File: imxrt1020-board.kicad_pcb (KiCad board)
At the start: 2 copper layers, 102.9 x 68.6 mm, 187 parts, among them J1 Micro_SD_Card_Det, J10 CASTELATED, J11 CASTELATED, J12 CASTELATED, J13 CASTELATED, J14 CASTELATED, J15 CASTELATED, J16 CASTELATED, J17 CASTELATED, J18 CASTELATED, J19 CASTELATED, J2 USB_OTG, J20 CASTELATED, J21 CASTELATED, J22 CASTELATED, J23 CASTELATED, J24 CASTELATED, J25 CASTELATED, J26 CASTELATED, J27 CASTELATED, J28 CASTELATED, J29 CASTELATED, J3 Conn_02x20_Odd_Even, J30 CASTELATED, J31 CASTELATED, J32 CASTELATED, J33 CASTELATED, J34 CASTELATED, J35 CASTELATED, J36 CASTELATED, J37 CASTELATED, J38 CASTELATED, J39 CASTELATED, J4 CASTELATED, J40 CASTELATED, J41 CASTELATED, J42 CASTELATED, J43 CASTELATED, J44 GS2, J45 GS2, J46 PWR_IN, J47 JTAG, J48 Conn_01x06, J49 CASTELATED, J5 CASTELATED, J50 CASTELATED, J51 CASTELATED, J52 CASTELATED, J53 CASTELATED, J54 CASTELATED, J55 CASTELATED, J56 CASTELATED, J57 CASTELATED, J58 RJ45-TRANSFO, J59 CASTELATED, J6 CASTELATED, J60 CASTELATED, J61 CASTELATED, J62 CASTELATED, J63 CASTELATED, J64 CASTELATED, J65 CASTELATED, J66 CASTELATED, J67 CASTELATED, J68 CASTELATED, J7 CASTELATED, J8 CASTELATED, J9 CASTELATED, SW1 RST, SW2 SW_DIP_x02, SW3 WAKE, U1 imx_rt1020-qfp144, U2 M25PX32-VMW, U3 AS4C16M16S, U4 TPS3839DBZ, U5 LM1084-3.3, U6 ISL3178E, U7 KSZ8081RNA, U8 TCAN332D, Y1 24MHz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

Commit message: Add USB EMI filter, more silkscreen enances
Signed-off-by: Martin Ribelotta <martinribelotta@gmail.com>
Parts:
- added U9: NUF2221W1http, TO_SOT_Packages_SMD:SOT-363_SC-70-6, F.Cu at (116.1, 117.8)
- moved J44 6.09 mm to (116.9, 127.7), turned to 90 degrees
- moved J45 4.14 mm to (116.9, 122.7), turned to 270 degrees
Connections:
- U1 pad 62: /GPIO/OTG_D- -> /GPIO/A_OTG_D-
- U1 pad 63: /GPIO/OTG_D+ -> /GPIO/A_OTG_D+
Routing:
- net +3V3: track 588.6 -> 643.7 mm, vias 3 -> 5
- net /GPIO/OTG_D-: track 60.1 -> 20.2 mm, vias 2 -> 1
- net /GPIO/A_OTG_D-: track 0.00 -> 38.9 mm, vias 0 -> 2
- net /GPIO/OTG_D+: track 59.8 -> 21.1 mm, vias 2 -> 1
- net /GPIO/A_OTG_D+: track 0.00 -> 37.5 mm, vias 0 -> 2
- net GND: track 451.0 -> 466.3 mm, vias 284 -> 280
- net /POWER/PWR_IN1: track 12.0 -> 17.5 mm, vias 6 -> 7
- net +5V: track 37.9 -> 41.3 mm
- net /GPIO/DC_IN: track 5.26 -> 5.93 mm
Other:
- board text added: "+5V +3v3 IO31 IO30 IO29 IO28 IO27 IO26 IO25 IO24 IO23 IO22 IO21 IO20 IO19 IO18 IO17 IO16 IO07 IO06"
- board text removed: "IO31 IO30 IO29 IO28 IO27 IO26 IO25 IO24 IO23 IO22 IO21 IO20 IO19 IO18 IO17 IO16 IO07 IO06"

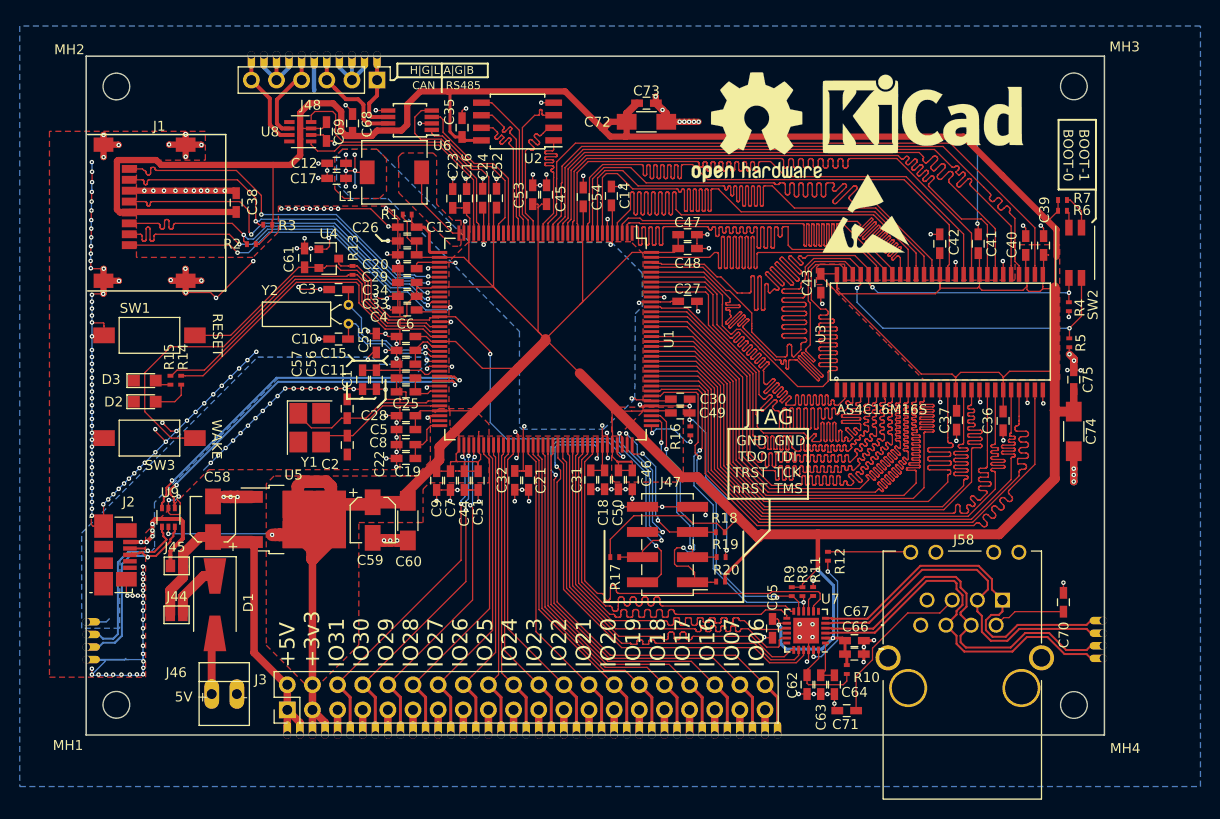
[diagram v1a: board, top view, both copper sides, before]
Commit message: Minor changes on PCB
Signed-off-by: Martin Ribelotta <martinribelotta@gmail.com>
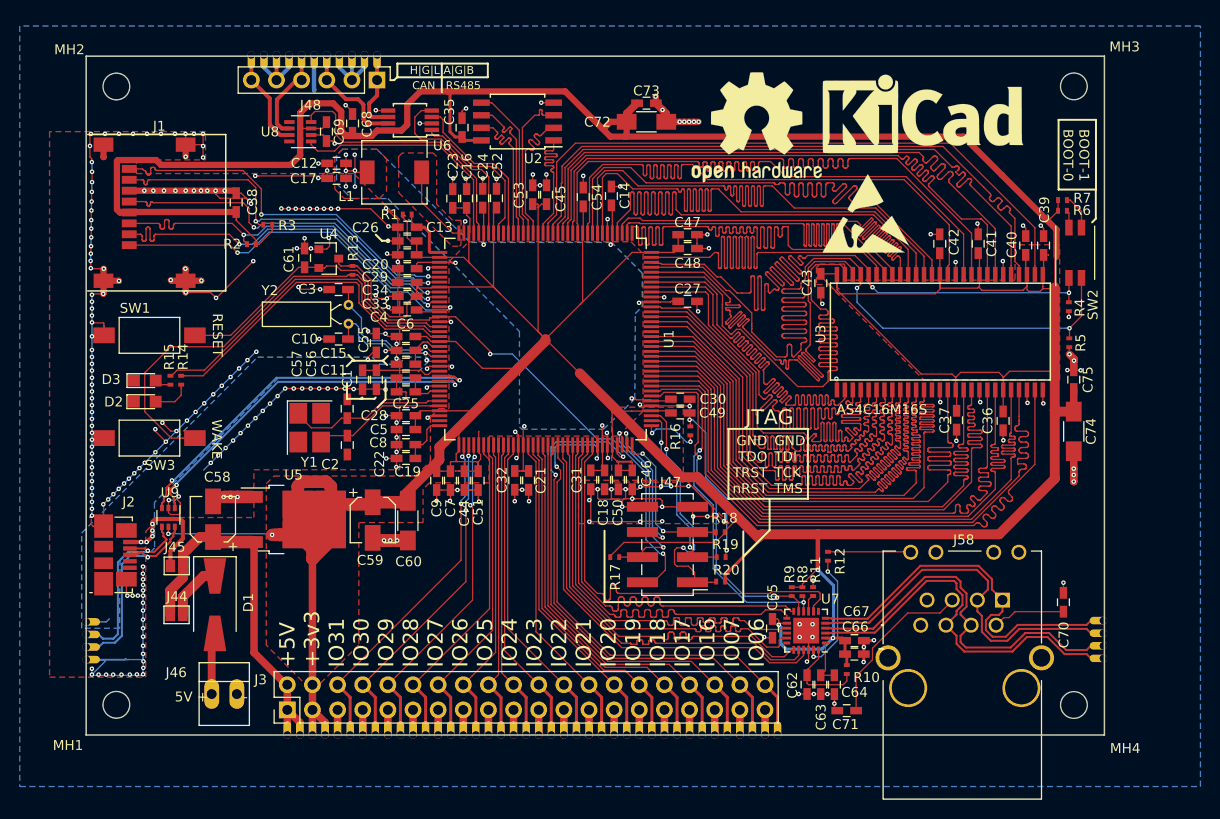
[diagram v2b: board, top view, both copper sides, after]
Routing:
- net GND: track 466.3 -> 520.6 mm, vias 280 -> 298
- net +3V3: track 643.7 -> 639.3 mm
- net /GPIO/JTAG_nRST: track 75.9 -> 72.4 mm
- net /MEMORY/SD_CLK: track 38.0 -> 37.0 mm
- net /GPIO/JTAG_TDO: track 14.8 -> 15.6 mm
- net /GPIO/JTAG_TRST: track 19.2 -> 19.9 mm
- net /MEMORY/SD_D0: track 38.9 -> 39.5 mm

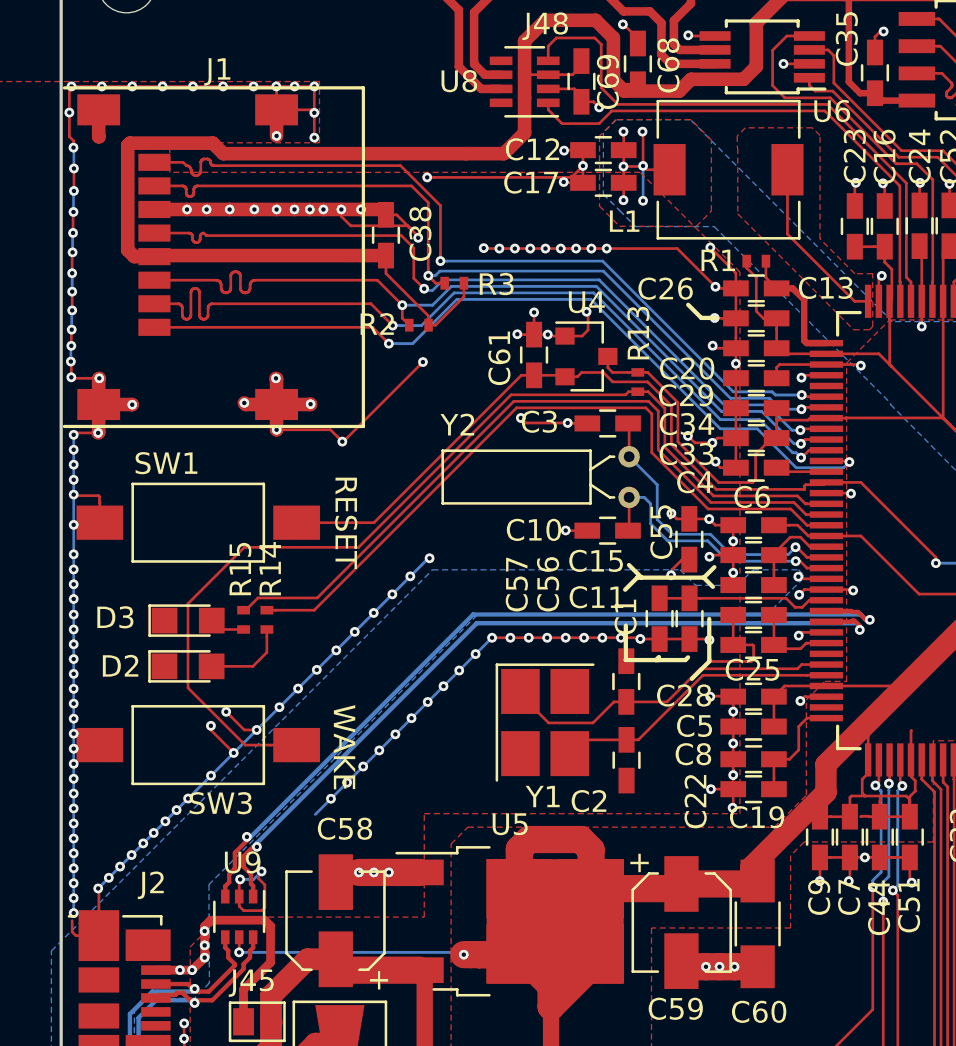
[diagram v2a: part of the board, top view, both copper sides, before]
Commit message: Change oscilators footprints and types matching ref design
Signed-off-by: Martin Ribelotta <martinribelotta@gmail.com>
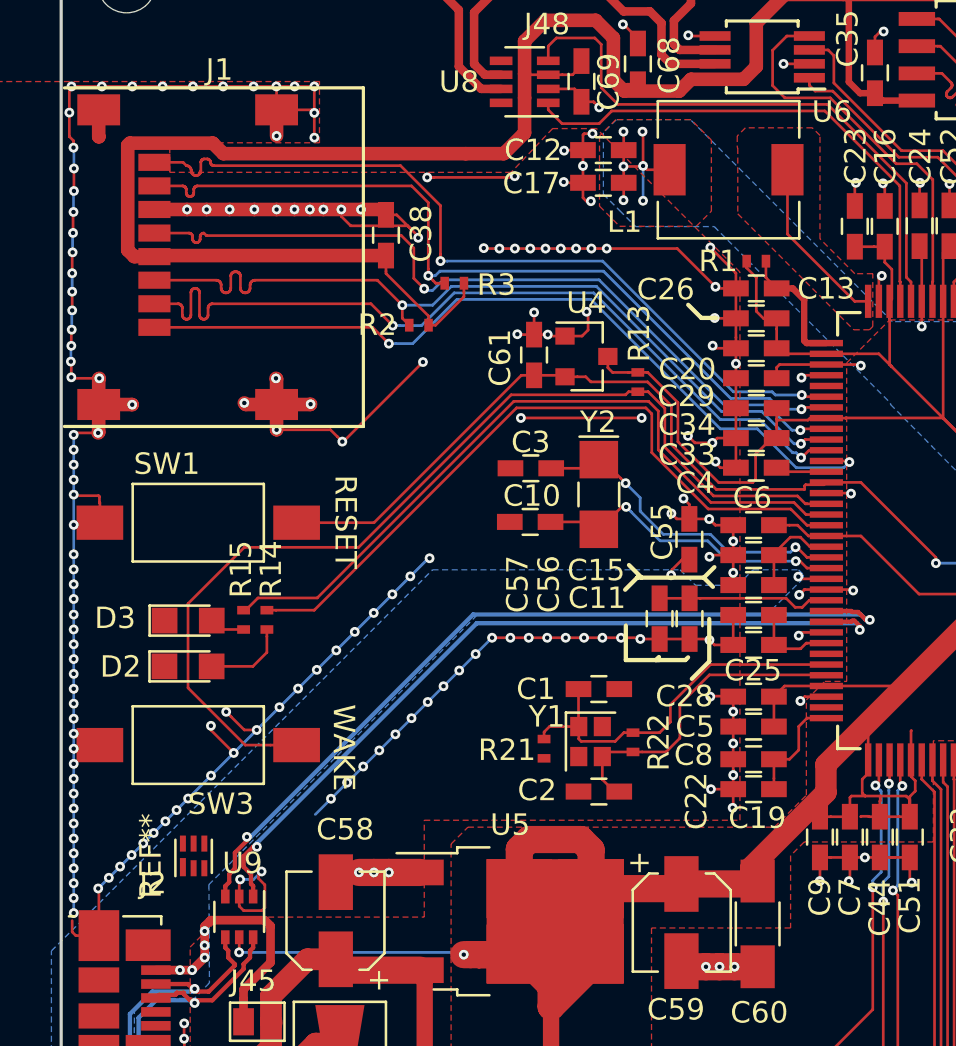
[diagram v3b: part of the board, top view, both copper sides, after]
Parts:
- added R21: 2.2M, Resistors_SMD:R_0402_NoSilk, F.Cu at (130.3, 110.0)
- added R22: 1M, Resistors_SMD:R_0402_NoSilk, F.Cu at (134.5, 109.7)
- added REF**: WSON6_1.5x1.5mm_Pitch0.5mm, Housings_SON:WSON6_1.5x1.5mm_Pitch0.5mm, F.Cu at (114.0, 115.0)
- Y1: footprint Crystals:Crystal_SMD_3225-4pin_3.2x2.5mm_HandSoldering -> Crystals:Crystal_SMD_2016-4pin_2.0x1.6mm
- Y2: footprint Crystals:Crystal_C26-LF_d2.1mm_l6.5mm_Horizontal -> Crystals:Crystal_SMD_MicroCrystal_CC7V-T1A-2pin_3.2x1.5mm_HandSoldering
- moved C3 4.15 mm to (129.7, 96.9)
- moved C10 3.64 mm to (129.7, 99.4)
- moved Y1 2.30 mm to (132.5, 109.7)
- moved Y2 2.26 mm to (132.9, 98.1)
- moved C2 1.95 mm to (132.9, 112.0), turned to 180 degrees
- moved C1 1.33 mm to (132.9, 107.2), turned to 0 degrees
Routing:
- net GND: track 520.6 -> 508.9 mm, vias 298 -> 297
- net (no net): track 0.00 -> 10.1 mm, vias 0 -> 4
- net Net-(C10-Pad1): track 12.7 -> 14.6 mm, vias 1 -> 2
- net Net-(C1-Pad1): track 16.1 -> 17.9 mm
- net Net-(C2-Pad1): track 13.5 -> 15.1 mm
- net Net-(C3-Pad1): track 14.0 -> 15.5 mm, vias 1 -> 2

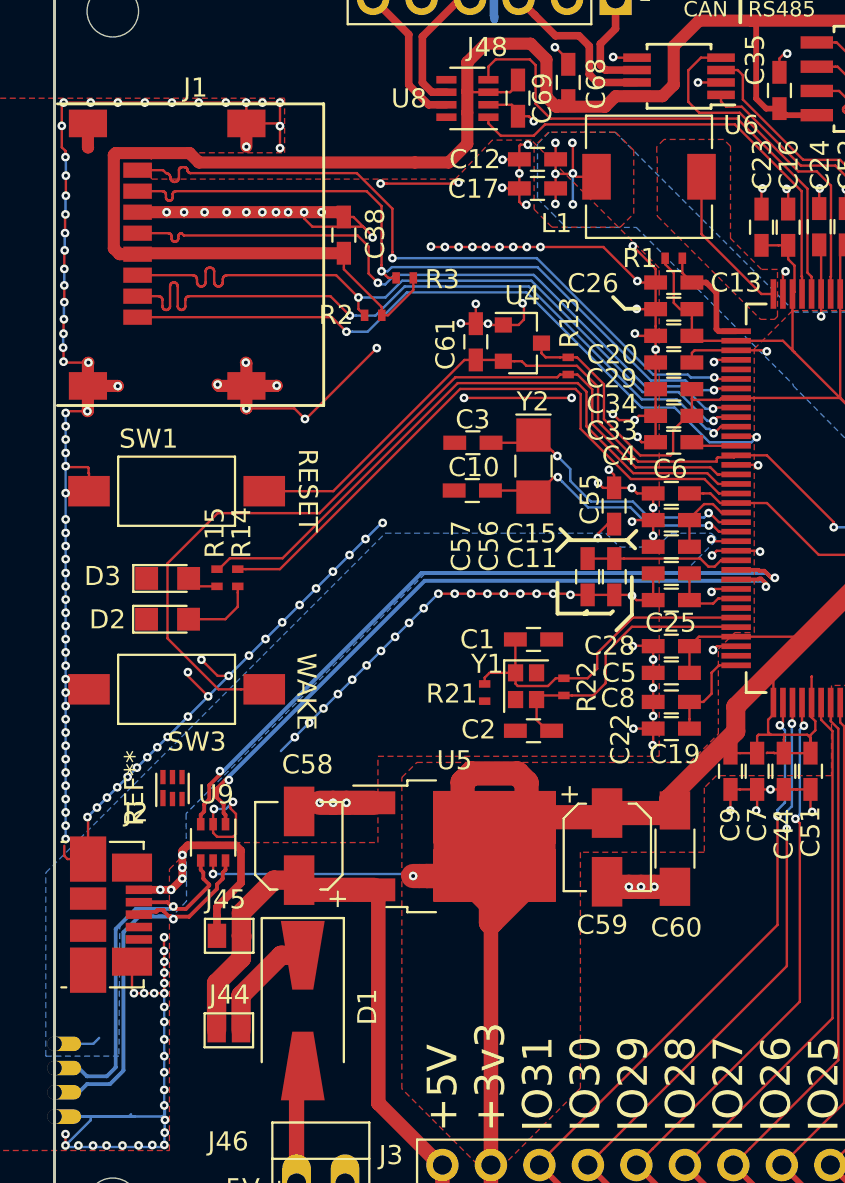
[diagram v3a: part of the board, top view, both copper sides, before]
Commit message: Enance USB EMI and filter circuit. Replace L1 (DC/DC) with correct part-number
Signed-off-by: Martin Ribelotta <martinribelotta@gmail.com>
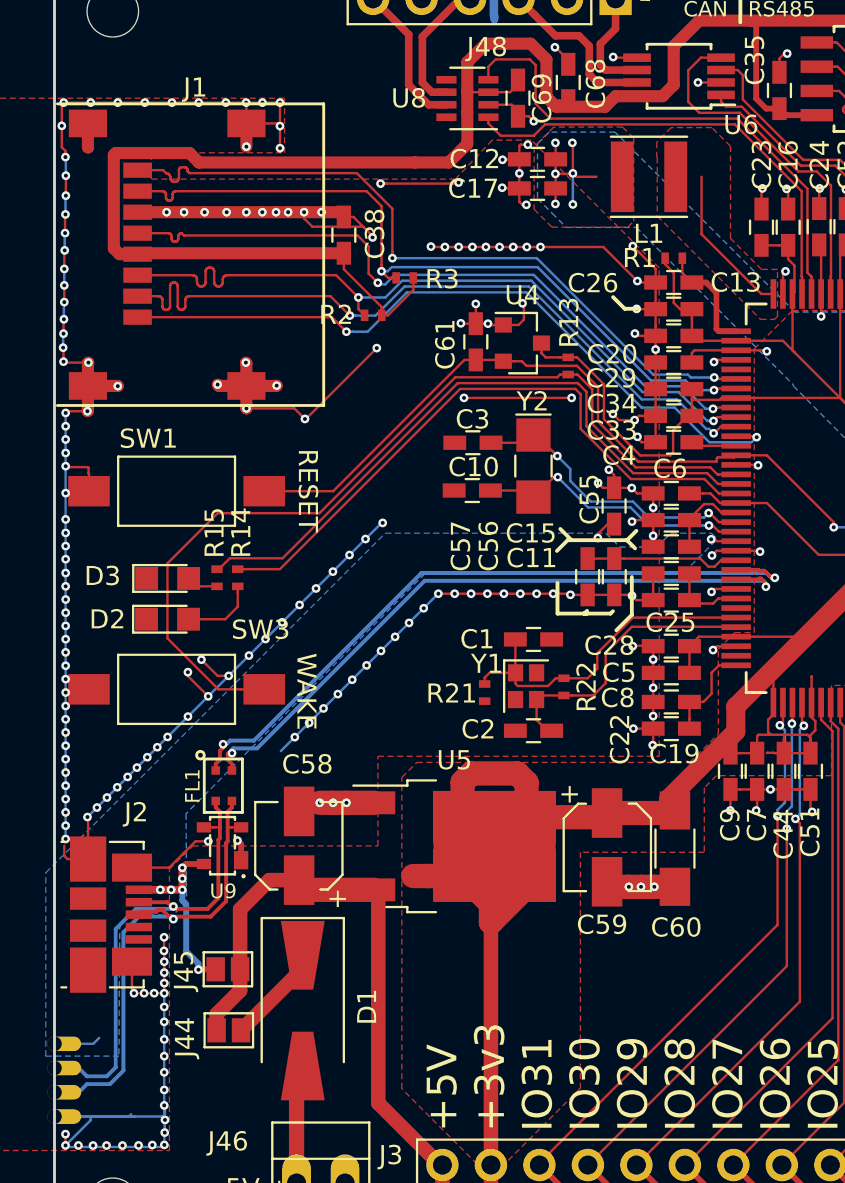
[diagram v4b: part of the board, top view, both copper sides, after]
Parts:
- removed REF**: WSON6_1.5x1.5mm_Pitch0.5mm, Housings_SON:WSON6_1.5x1.5mm_Pitch0.5mm
- added FL1: DLW21HN900SQ2L, local:SRF2012, F.Cu at (116.2, 114.1)
- J58: value RJ45-TRANSFO -> SI-50196-F
- L1: footprint Inductors_SMD:L_6.3x6.3_H3 -> Inductors_SMD:L_Taiyo-Yuden_MD-4040
- U9: value NUF2221W1http -> PRTR5V0U2X; footprint TO_SOT_Packages_SMD:SOT-363_SC-70-6 -> local:SOT-143-4
- moved J45 1.75 mm to (116.9, 124.5)
- moved U9 0.52 mm to (116.6, 118.0), turned to 90 degrees
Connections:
- U9 pad 1: /GPIO/A_OTG_D+ -> GND
- U9 pad 2: GND -> /GPIO/OTG_D+
- U9 pad 3: /GPIO/A_OTG_D- -> /GPIO/OTG_D-
- U9 pad 4: /GPIO/OTG_D- -> /POWER/PWR_IN1
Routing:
- net +3V3: track 639.3 -> 628.1 mm, vias 5 -> 3
- net /GPIO/OTG_D-: track 20.2 -> 24.9 mm
- net /GPIO/OTG_D+: track 21.1 -> 25.7 mm
- net /GPIO/A_OTG_D+: track 37.5 -> 35.1 mm
- net /GPIO/A_OTG_D-: track 38.9 -> 36.5 mm
- net /POWER/PWR_IN1: track 17.5 -> 15.3 mm, vias 7 -> 8
- net /GPIO/DC_IN: track 5.93 -> 5.27 mm

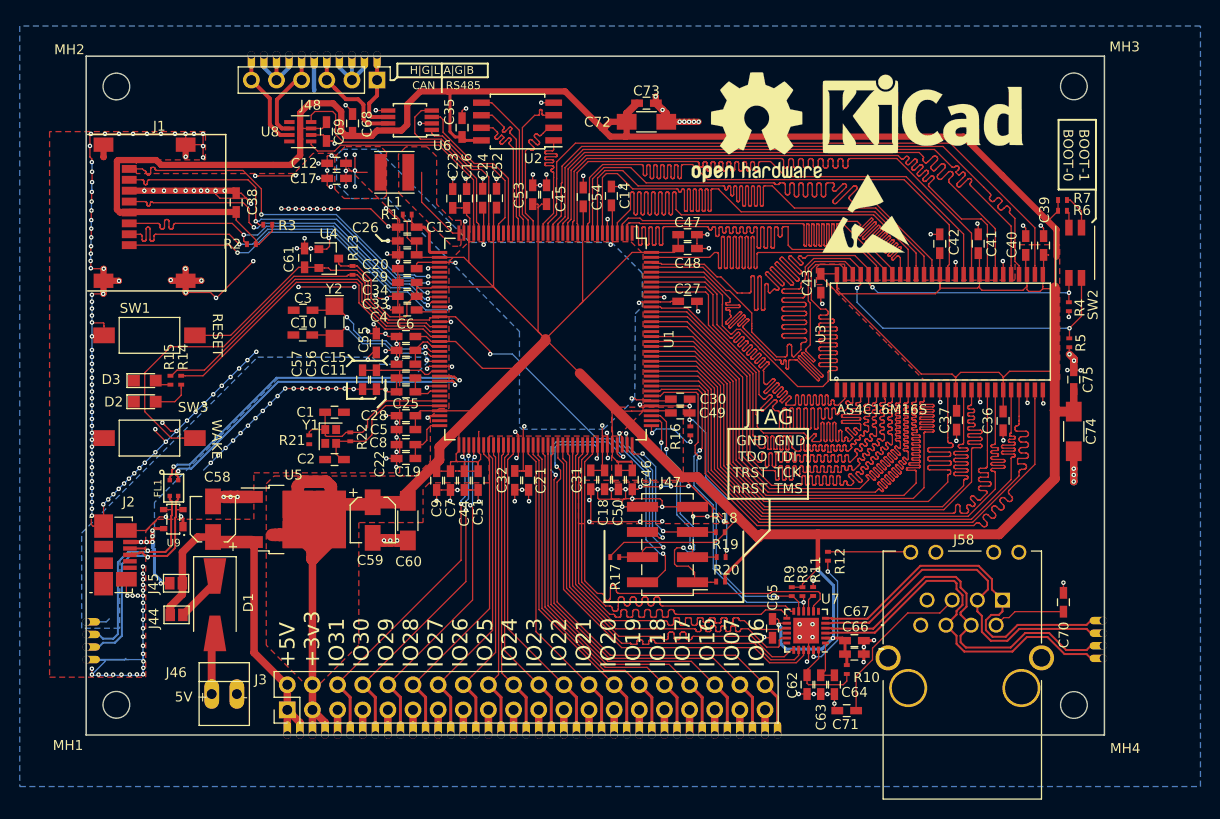
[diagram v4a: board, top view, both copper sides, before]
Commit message: Change R/C to 0402 footprint
Signed-off-by: Martin Ribelotta <martinribelotta@gmail.com>
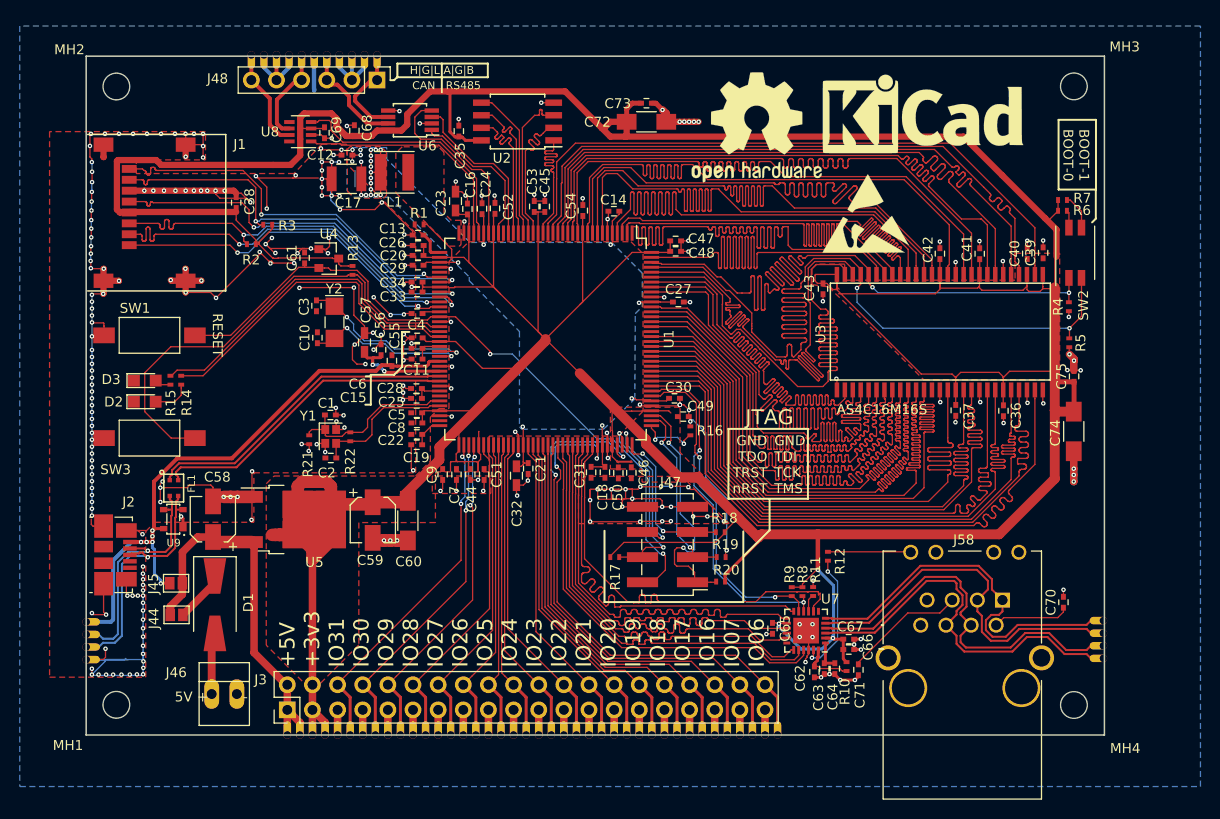
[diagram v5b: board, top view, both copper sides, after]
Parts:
- C1, C10, C11, C12, C13, C14, C15, C16, C18, C19, C2, C20, C21, C22, C24, C25, C26, C27, C28, C29, C3, C30, C31, C33, C34, C35, C36, C37, C38, C39, C4, C40, C41, C42, C43, C44, C45, C46, C47, C48, C49, C5, C50, C51, C52, C53, C54, C55, C56, C6, C61, C62, C63, C64, C65, C66, C67, C68, C69, C7, C70, C71, C73, C75, C8, C9: footprint Capacitors_SMD:C_0603_HandSoldering -> Capacitors_SMD:C_0402
- C17: footprint Capacitors_SMD:C_0603_HandSoldering -> Capacitors_SMD:C_1210
- moved C71 4.29 mm to (185.8, 133.2), turned to 270 degrees
- moved C57 3.77 mm to (135.9, 100.2), turned to 90 degrees
- moved C56 3.06 mm to (137.6, 100.9), turned to 90 degrees
- moved C55 2.38 mm to (138.7, 102.0)
- moved C19 1.76 mm to (141.2, 110.5)
- moved C63 1.65 mm to (182.3, 133.1)
- moved C64 1.62 mm to (183.4, 133.1)
- moved C14 1.56 mm to (161.1, 86.9), turned to 180 degrees
- moved R1 1.56 mm to (141.4, 88.2), turned to 180 degrees
- moved C22 1.50 mm to (141.2, 109.5)
- moved C28 1.50 mm to (141.1, 104.8)
- moved C10 1.50 mm to (131.1, 99.7), turned to 90 degrees
- moved C62 1.48 mm to (181.3, 133.4)
- moved C3 1.42 mm to (131.0, 96.5), turned to 270 degrees
- moved C54 1.37 mm to (157.9, 86.8)
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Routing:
- net /POWER/PWR_IN1: track 15.3 -> 61.8 mm, vias 8 -> 6
- net +3V3: track 628.1 -> 605.9 mm
- net (no net): track 10.1 -> 0.00 mm, vias 4 -> 0
- net Net-(L1-Pad1): track 8.07 -> 0.00 mm
- net /POWER/DCDC_OUT: track 41.9 -> 48.5 mm, vias 13 -> 27
- net Net-(C71-Pad1): track 17.1 -> 12.3 mm
- net /GPIO/A_OTG_D-: track 36.5 -> 32.1 mm, vias 2 -> 0
- net /GPIO/A_OTG_D+: track 35.1 -> 31.4 mm, vias 2 -> 0
- net Net-(C62-Pad1): track 8.81 -> 5.33 mm
- net /MEMORY/SD_CMD: track 38.8 -> 42.0 mm
- net Net-(C3-Pad1): track 15.5 -> 18.3 mm
- net /MEMORY/SD_CLK: track 37.0 -> 39.6 mm
- net /MEMORY/SD_D0: track 39.5 -> 42.0 mm
- net /MEMORY/SD_D2: track 38.1 -> 35.8 mm
- net Net-(C56-Pad1): track 8.09 -> 10.2 mm, vias 0 -> 2
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- removed copper zone on B.Cu, net /POWER/PWR_IN1
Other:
- board text removed: "WAKE"
